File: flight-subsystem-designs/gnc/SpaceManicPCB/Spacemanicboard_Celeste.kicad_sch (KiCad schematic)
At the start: 1 part

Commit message: Final Changes
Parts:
- removed H17: Radio Connector, Connector_Molex:CON_MolexSlimStack_54363-0689, symbol Connector_Generic:Conn_02x30_Odd_Even
- added H18: GPS Connector, Connector_Molex:CON_MolexSlimStack_54363-0689, symbol Connector_Generic:Conn_02x30_Odd_Even
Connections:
- net 3.3V_S: now also H18.10 (Pin_10), H18.8 (Pin_8), H18.9 (Pin_9)
- net 5V_S: now also H18.3 (Pin_3), H18.4 (Pin_4), H18.5 (Pin_5), H18.6 (Pin_6)
- net CAN_N: now also H18.28 (Pin_28)
- net CAN_P: now also H18.26 (Pin_26)
- net GND: now also H18.11 (Pin_11), H18.12 (Pin_12), H18.23 (Pin_23), H18.24 (Pin_24), H18.29 (Pin_29), H18.30 (Pin_30), H18.47 (Pin_47), H18.48 (Pin_48), H18.7 (Pin_7)
- net RS485_N: now also H18.18 (Pin_18)
- net RS485_P: now also H18.16 (Pin_16)
- new net PPS: H18.46 (Pin_46)
- new net RST_Celeste: H18.45 (Pin_45)
- no-connect marks 37 -> 38

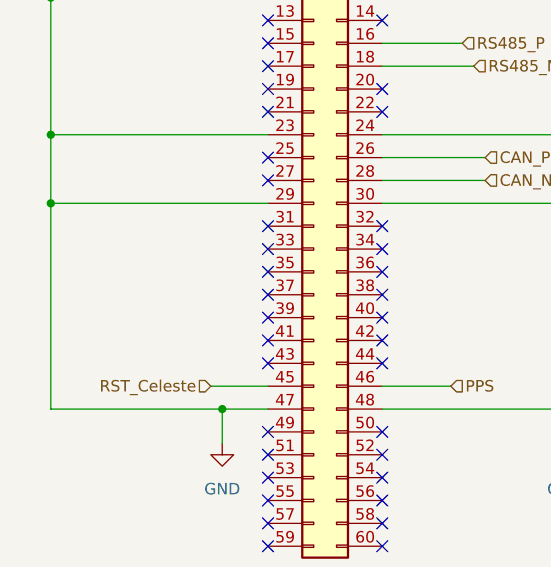
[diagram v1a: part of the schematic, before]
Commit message: Added UART
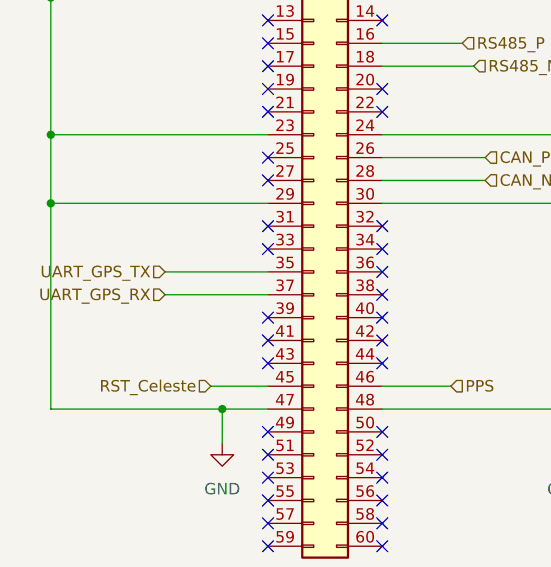
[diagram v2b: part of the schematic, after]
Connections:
- net UART_GPS_TX: now reaches H18.35 (Pin_35)
- net UART_GPS_RX: now reaches H18.37 (Pin_37)
- no-connect marks 38 -> 36
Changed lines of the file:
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@@
-	)
-	(no_connect
-		(at 111.76 109.22)
 	)
 	(no_connect
@@
 	)
 	(no_connect
-		(at 111.76 111.76)
-	)
-	(no_connect
 		(at 111.76 116.84)
 	)
@@
 	(wire
 		(pts
+			(xy 100.33 109.22) (xy 111.76 109.22)
+		)
+		(stroke
+			(width 0)
+			(type default)
+		)
+	)
+	(wire
+		(pts
 			(xy 106.68 124.46) (xy 106.68 128.27)
 		)
@@
 		(pts
 			(xy 127 68.58) (xy 127 71.12)
+		)
+		(stroke
+			(width 0)
+			(type default)
+		)
+	)
+	(wire
+		(pts
+			(xy 100.33 111.76) (xy 111.76 111.76)
 		)
 		(stroke
@@
 		)
 	)
+	(hierarchical_label "UART_GPS_TX"
+		(shape input)
+		(at 100.33 109.22 180)
+		(effects
+			(font
+				(size 1.27 1.27)
+			)
+			(justify right)
+		)
+	)
 	(hierarchical_label "RS485_P"
 		(shape input)
@@
 		)
 	)
+	(hierarchical_label "UART_GPS_RX"
+		(shape input)
+		(at 100.33 111.76 180)
+		(effects
+			(font
+				(size 1.27 1.27)
+			)
+			(justify right)
+		)
+	)
